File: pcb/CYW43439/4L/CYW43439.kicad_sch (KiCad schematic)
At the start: 36 parts, among them J1 GPIOs, J2 SPI, J3 Power, J4 RP-SMA Female, U1 CYW43439KUBGT, Y1 Crystal

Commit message: [pcb] add USB-A
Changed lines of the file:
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@@
 (kicad_sch
-	(version 20231120)
+	(version 20250114)
 	(generator "eeschema")
-	(generator_version "8.0")
+	(generator_version "9.0")
 	(paper "A4")
 	(junction
@@
 		)
 	)
+	(embedded_fonts no)
 )

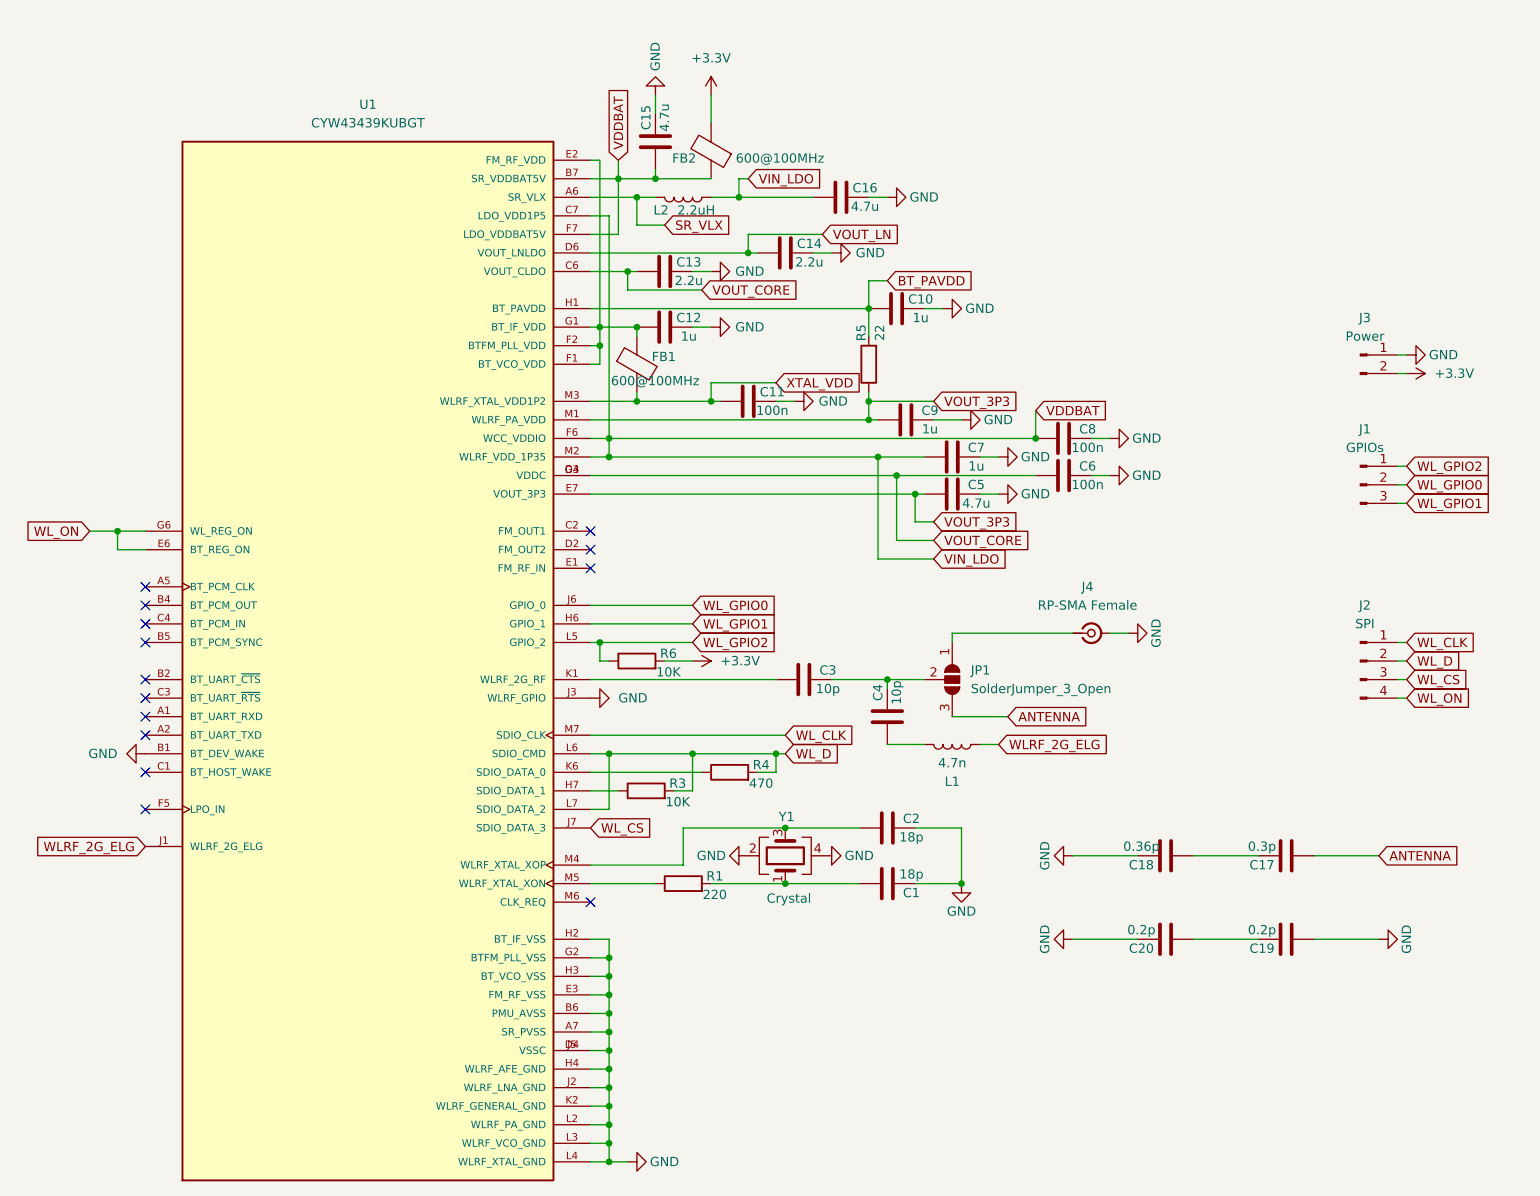
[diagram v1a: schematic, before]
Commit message: [CYW43439] fix VDDBAT/LDO_IN short circuited, others
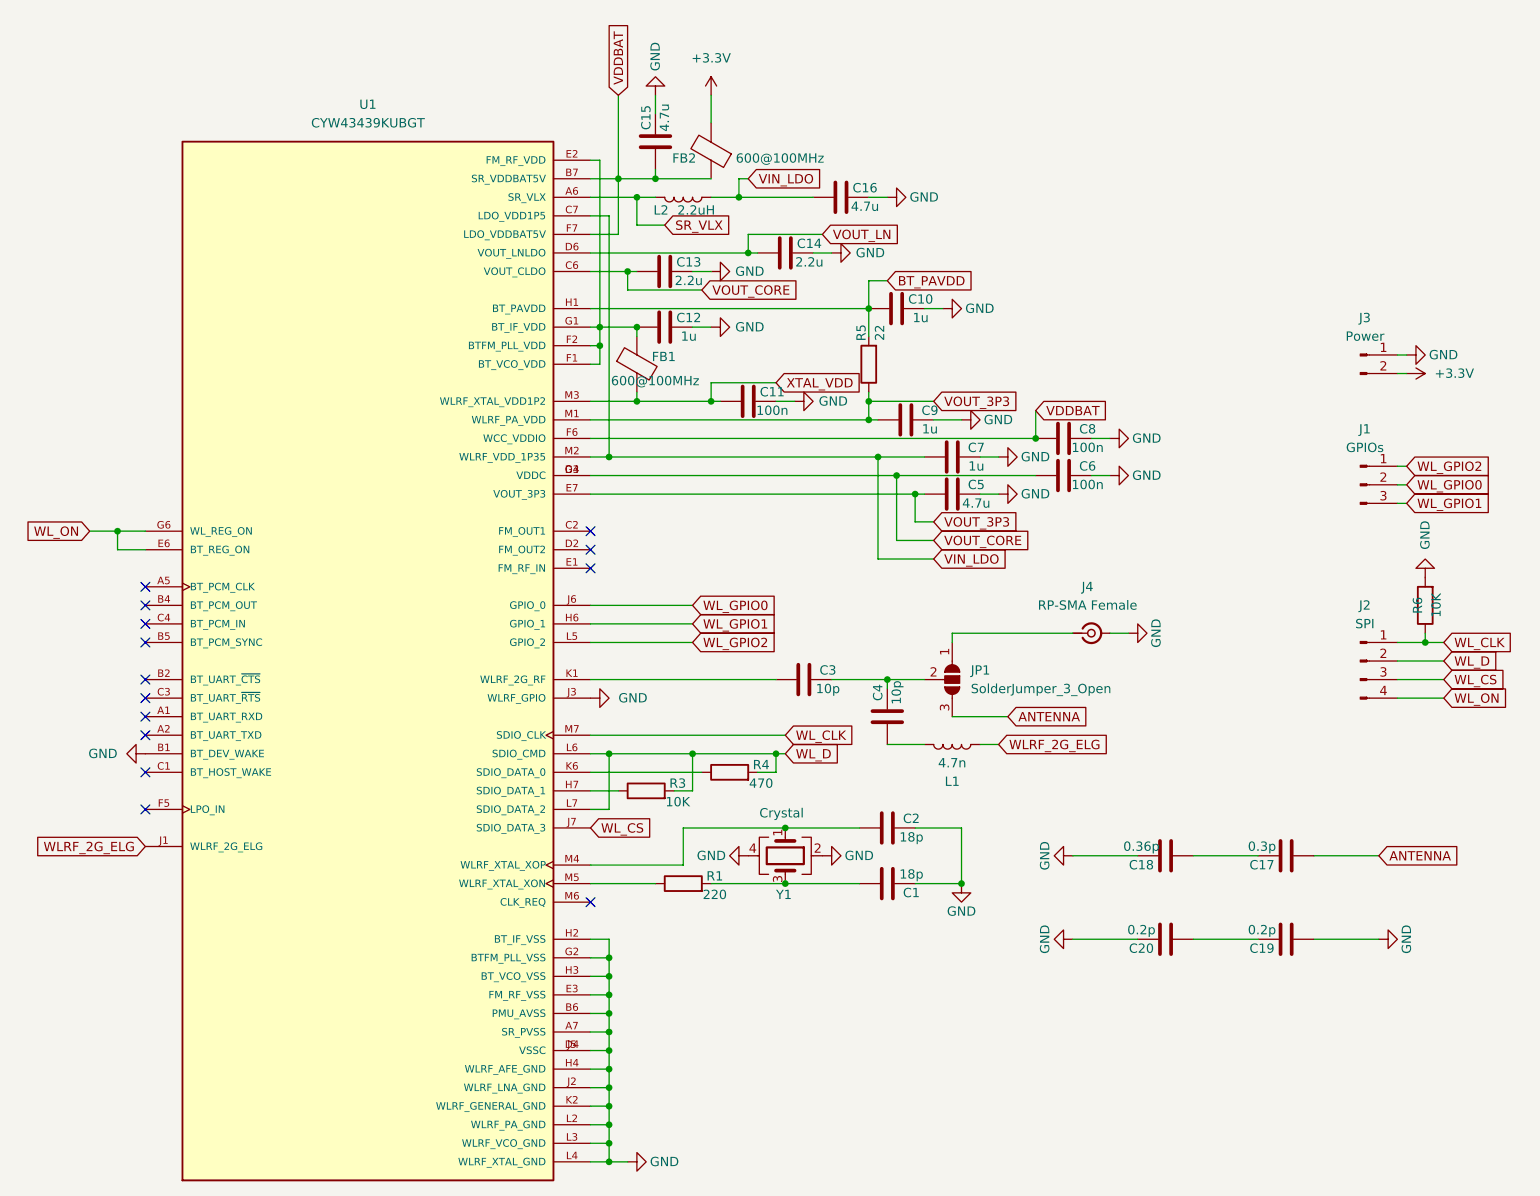
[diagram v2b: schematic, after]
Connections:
- net +3.3V: no longer R6.2
- net GND: now also R6.2
- net VDDBAT: no longer C16.1, C7.1, L2.1, U1.C7 (LDO_VDD1P5), U1.M2 (WLRF_VDD_1P35)
- net WL_CLK: now also R6.1
- net WL_GPIO2: no longer R6.1
- net at C2.1, U1.M4 (WLRF_XTAL_XOP): now also Y1.1; no longer Y1.3
- net at C1.1, R1.2: now also Y1.3; no longer Y1.1
- new net VIN_LDO: C16.1, C7.1, L2.1, U1.C7 (LDO_VDD1P5), U1.M2 (WLRF_VDD_1P35)
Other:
- moved on the sheet: Y1
